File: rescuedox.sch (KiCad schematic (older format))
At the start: 84 parts, among them SW110 SW_Push_45deg, SW111 SW_Push_45deg, SW112 SW_Push_45deg, SW113 SW_Push_45deg, SW114 SW_Push_45deg, SW115 SW_Push_45deg, SW116 SW_Push_45deg, SW18 SW_Push_45deg, SW19 SW_Push_45deg, SW210 SW_Push_45deg, SW211 SW_Push_45deg, SW212 SW_Push_45deg, SW213 SW_Push_45deg, SW214 SW_Push_45deg, SW215 SW_Push_45deg, SW216 SW_Push_45deg, SW28 SW_Push_45deg, SW29 SW_Push_45deg, SW310 SW_Push_45deg, SW311 SW_Push_45deg, SW312 SW_Push_45deg, SW313 SW_Push_45deg, SW314 SW_Push_45deg, SW315 SW_Push_45deg, SW316 SW_Push_45deg, SW38 SW_Push_45deg, SW39 SW_Push_45deg, SW410 SW_Push_45deg, SW411 SW_Push_45deg, SW412 SW_Push_45deg, SW413 SW_Push_45deg, SW415 SW_Push_45deg, SW48 SW_Push_45deg, SW49 SW_Push_45deg, SW510 SW_Push_45deg, SW511 SW_Push_45deg, SW512 SW_Push_45deg, SW514 SW_Push_45deg, SW515 SW_Push_45deg, SW516 SW_Push_45deg, SW58 SW_Push_45deg, SW59 SW_Push_45deg

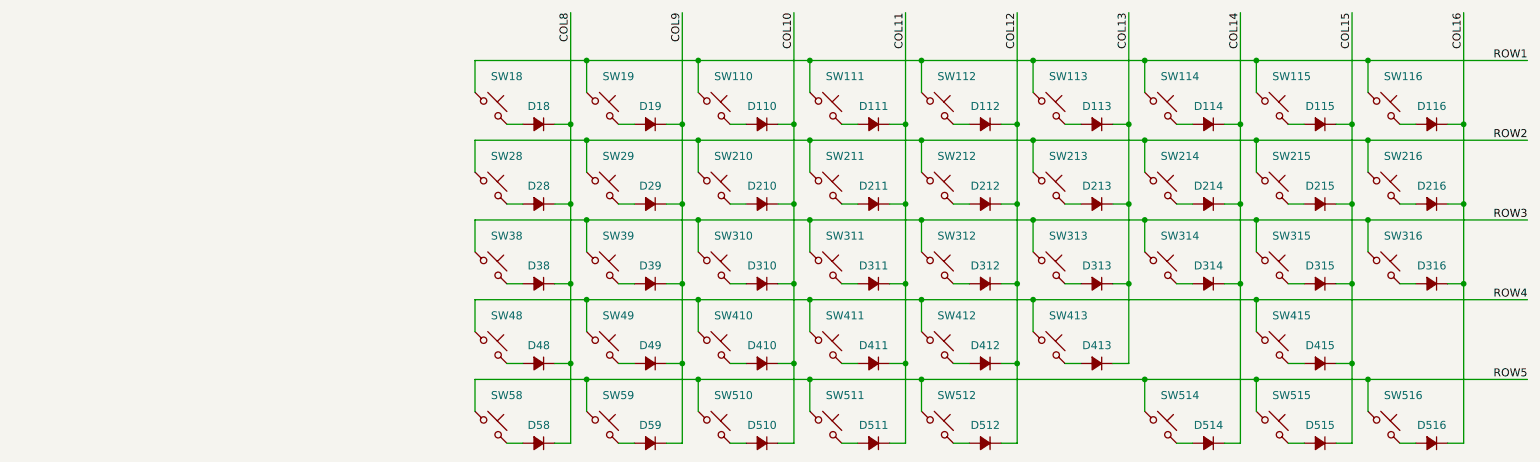
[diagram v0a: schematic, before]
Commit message: Separate left/right sheets, draw left-side matrix
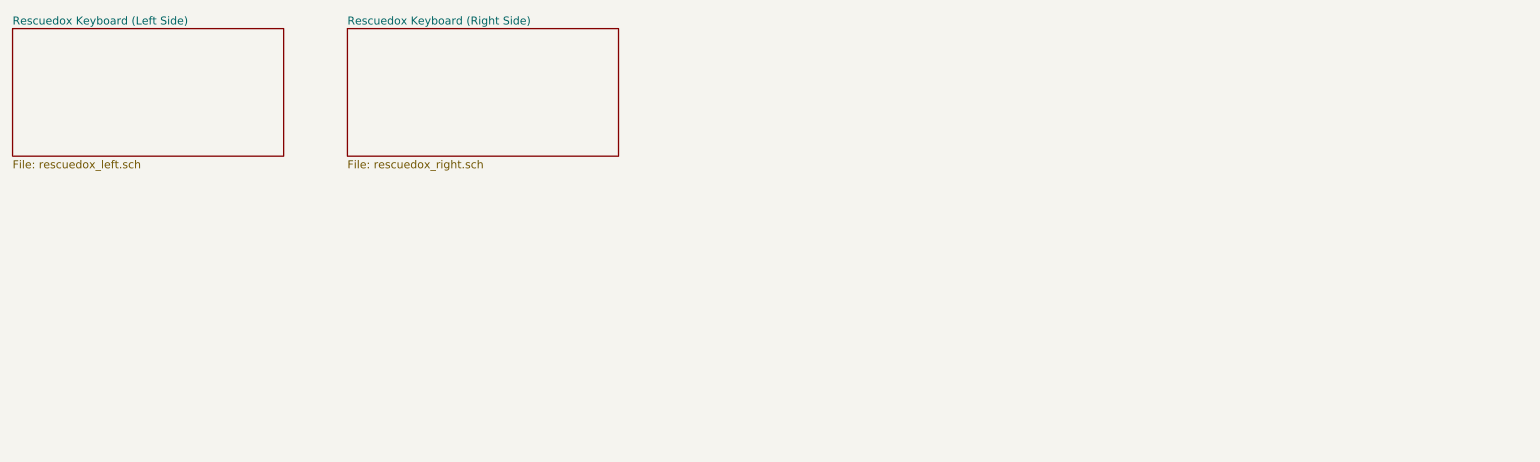
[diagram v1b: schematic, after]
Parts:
- removed D110, D111, D112, D113, D114, D115, D116, D18, D19, D210, D211, D212, D213, D214, D215, D216, D28, D29, D310, D311, D312, D313, D314, D315, D316, D38, D39, D410, D411, D412, D413, D415, D48, D49, D510, D511, D512, D514, D515, D516, D58, D59: D_Small_ALT, symbol Device:D_Small_ALT
- removed SW110, SW111, SW112, SW113, SW114, SW115, SW116, SW18, SW19, SW210, SW211, SW212, SW213, SW214, SW215, SW216, SW28, SW29, SW310, SW311, SW312, SW313, SW314, SW315, SW316, SW38, SW39, SW410, SW411, SW412, SW413, SW415, SW48, SW49, SW510, SW511, SW512, SW514, SW515, SW516, SW58, SW59: SW_Push_45deg, symbol Switch:SW_Push_45deg
